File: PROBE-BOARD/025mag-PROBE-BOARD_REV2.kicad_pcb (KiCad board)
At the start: 2 copper layers, 15 x 26.7 mm, 12 parts, among them M31 MountingHole_3.2mm_M3, SW1 SW_Push_Open

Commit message: ADDED VIAS
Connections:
- REF** pad 2: (no net) -> SIGNAL
- REF** pad 3: (no net) -> GND
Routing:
- net SIGNAL: vias 1 -> 8
- net GND: vias 1 -> 8

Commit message: Cleanup previous revisions
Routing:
- net Net-(D1-Pad2): track 1.81 -> 3.44 mm

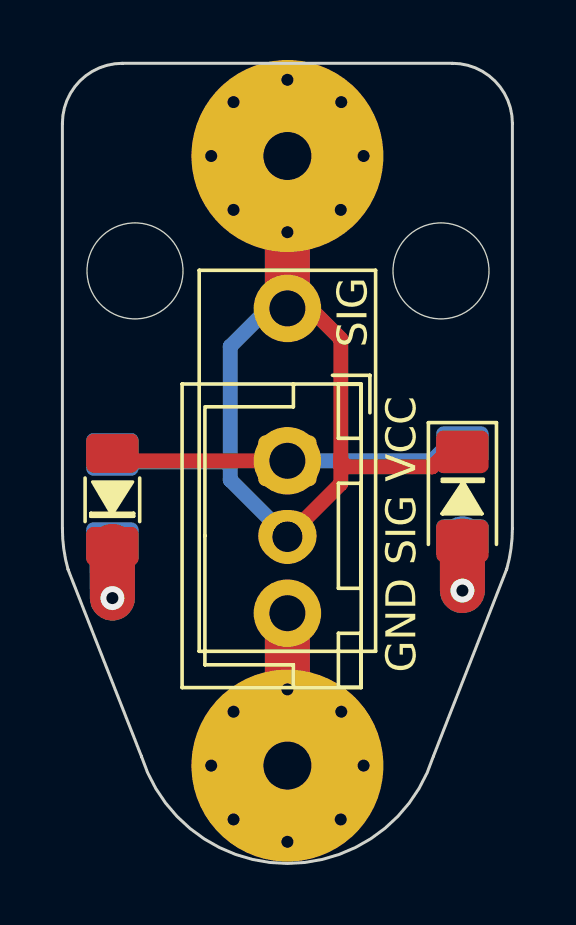
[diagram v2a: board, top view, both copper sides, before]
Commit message: Rev2a of vias
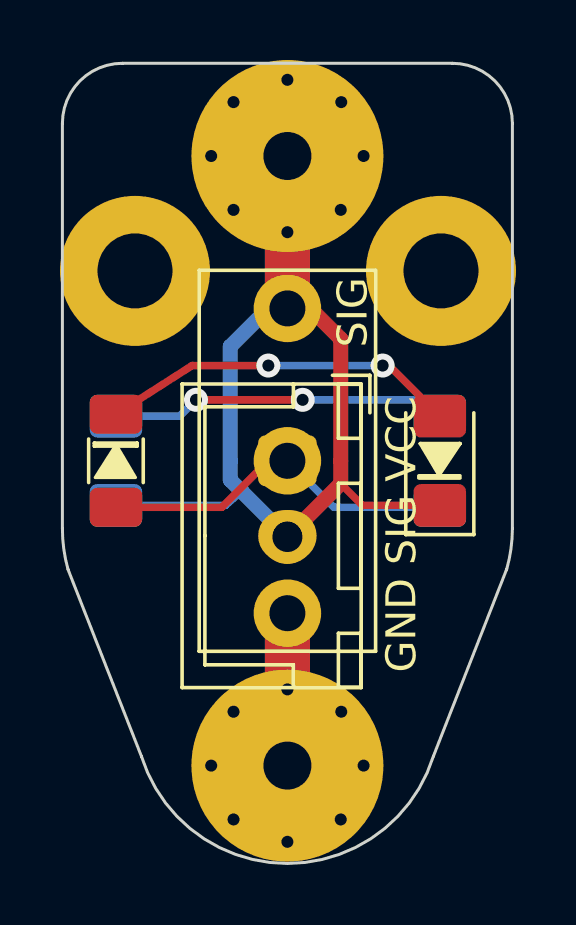
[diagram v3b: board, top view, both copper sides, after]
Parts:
- D1: moved to F.Cu
- D2: moved to B.Cu
- moved D2 11.6 mm to (-5.71, 0.00), turned to 90 degrees
- moved D1 11.0 mm to (5.08, 0.00), turned to 90 degrees
- moved R1 1.31 mm to (-5.71, 0.00), turned to 90 degrees
- moved R2 1.29 mm to (5.08, 0.00), turned to 90 degrees
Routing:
- net Net-(D1-Pad2): track 3.44 -> 12.0 mm, vias 1 -> 2
- net Net-(D2-Pad2): track 3.38 -> 11.2 mm, vias 1 -> 2
- net VCC: track 11.7 -> 12.4 mm
